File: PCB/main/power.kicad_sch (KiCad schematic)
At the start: 25 parts, among them IC1 MCP6002T-I_SN, IC2 ap2007, IC3 TP4056-42-ESOP8, IC4 LM3940IMP-3.3_NOPB, Q1 AO3401A

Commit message: Updated footprints
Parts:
- IC1: footprint SOIC127P600X175-8N -> EEE3088F_Footprints:SOIC127P600X175-8N
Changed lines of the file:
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@@
       (effects (font (size 1.27 1.27)) (justify left))
     )
-    (property "Footprint" "SOIC127P600X175-8N" (id 2) (at 97.155 132.08 0)
+    (property "Footprint" "EEE3088F_Footprints:SOIC127P600X175-8N" (id 2) (at 97.155 132.08 0)
       (effects (font (size 1.27 1.27)) (justify left) hide)
     )

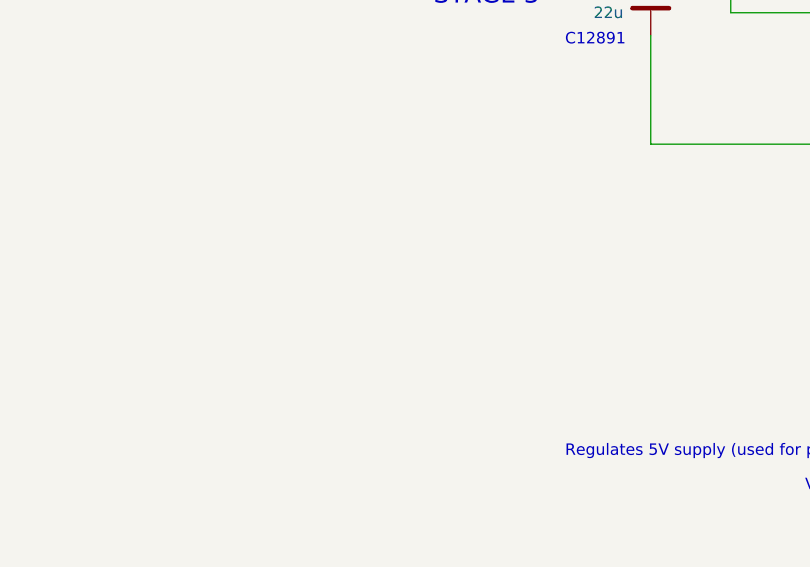
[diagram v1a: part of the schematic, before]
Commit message: Fixed a lot of shit. Added 3 test pads. Rounded PCB corners
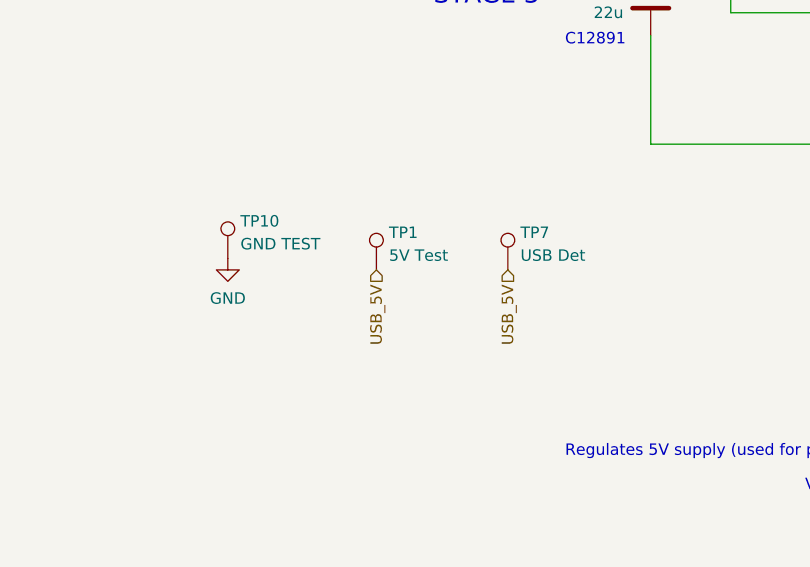
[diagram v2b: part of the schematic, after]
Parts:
- added TP1: 5V Test, TestPoint:TestPoint_Pad_2.5x2.5mm, symbol Connector:TestPoint
- added TP10: GND TEST, TestPoint:TestPoint_Pad_4.0x4.0mm, symbol Connector:TestPoint
- added TP7: USB Det, TestPoint:TestPoint_Pad_2.5x2.5mm, symbol Connector:TestPoint
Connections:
- net GND: now also TP10.1
- net USB_5V: now also TP1.1, TP7.1
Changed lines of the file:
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@@
     (effects (font (size 1.27 1.27)) (justify left))
   )
+  (hierarchical_label "USB_5V" (shape input) (at 161.29 95.885 270)
+    (effects (font (size 1.27 1.27)) (justify right))
+  )
   (hierarchical_label "5V" (shape input) (at 205.74 130.81 180)
     (effects (font (size 1.27 1.27)) (justify right))
@@
   )
   (hierarchical_label "GND" (shape input) (at 236.22 83.82 270)
+    (effects (font (size 1.27 1.27)) (justify right))
+  )
+  (hierarchical_label "USB_5V" (shape input) (at 175.895 95.885 270)
     (effects (font (size 1.27 1.27)) (justify right))
   )
@@
     (pin "2")
   )
+  (symbol (lib_id "Connector:TestPoint") (at 161.29 95.885 0) (unit 1)
+    (in_bom yes) (on_board yes) (fields_autoplaced)
+    (property "Reference" "TP1" (id 0) (at 162.687 91.7483 0)
+      (effects (font (size 1.27 1.27)) (justify left))
+    )
+    (property "Value" "5V Test" (id 1) (at 162.687 94.2852 0)
+      (effects (font (size 1.27 1.27)) (justify left))
+    )
+    (property "Footprint" "TestPoint:TestPoint_Pad_2.5x2.5mm" (id 2) (at 166.37 95.885 0)
+      (effects (font (size 1.27 1.27)) hide)
+    )
+    (property "Datasheet" "~" (id 3) (at 166.37 95.885 0)
+      (effects (font (size 1.27 1.27)) hide)
+    )
+    (pin "1")
+  )
   (symbol (lib_id "Device:LED") (at 43.18 50.8 90) (unit 1)
     (in_bom yes) (on_board yes)
@@
     (pin "1")
     (pin "2")
+  )
+  (symbol (lib_id "power:GND") (at 144.78 94.615 0) (unit 1)
+    (in_bom yes) (on_board yes) (fields_autoplaced)
+    (property "Reference" "#PWR0101" (id 0) (at 144.78 100.965 0)
+      (effects (font (size 1.27 1.27)) hide)
+    )
+    (property "Value" "GND" (id 1) (at 144.78 99.0584 0))
+    (property "Footprint" "" (id 2) (at 144.78 94.615 0)
+      (effects (font (size 1.27 1.27)) hide)
+    )
+    (property "Datasheet" "" (id 3) (at 144.78 94.615 0)
+      (effects (font (size 1.27 1.27)) hide)
+    )
+    (pin "1")
+  )
+  (symbol (lib_id "Connector:TestPoint") (at 144.78 94.615 0) (unit 1)
+    (in_bom yes) (on_board yes) (fields_autoplaced)
+    (property "Reference" "TP10" (id 0) (at 146.177 90.4783 0)
+      (effects (font (size 1.27 1.27)) (justify left))
+    )
+    (property "Value" "GND TEST" (id 1) (at 146.177 93.0152 0)
+      (effects (font (size 1.27 1.27)) (justify left))
+    )
+    (property "Footprint" "TestPoint:TestPoint_Pad_4.0x4.0mm" (id 2) (at 149.86 94.615 0)
+      (effects (font (size 1.27 1.27)) hide)
+    )
+    (property "Datasheet" "~" (id 3) (at 149.86 94.615 0)
+      (effects (font (size 1.27 1.27)) hide)
+    )
+    (pin "1")
   )
   (symbol (lib_id "AO3401A:AO3401A") (at 78.105 125.73 90) (unit 1)
@@
     (pin "2")
   )
+  (symbol (lib_id "Connector:TestPoint") (at 175.895 95.885 0) (unit 1)
+    (in_bom yes) (on_board yes) (fields_autoplaced)
+    (property "Reference" "TP7" (id 0) (at 177.292 91.7483 0)
+      (effects (font (size 1.27 1.27)) (justify left))
+    )
+    (property "Value" "USB Det" (id 1) (at 177.292 94.2852 0)
+      (effects (font (size 1.27 1.27)) (justify left))
+    )
+    (property "Footprint" "TestPoint:TestPoint_Pad_2.5x2.5mm" (id 2) (at 180.975 95.885 0)
+      (effects (font (size 1.27 1.27)) hide)
+    )
+    (property "Datasheet" "~" (id 3) (at 180.975 95.885 0)
+      (effects (font (size 1.27 1.27)) hide)
+    )
+    (pin "1")
+  )
   (symbol (lib_id "Device:R") (at 50.8 43.18 0) (unit 1)

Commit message: Updated PCB with testpads
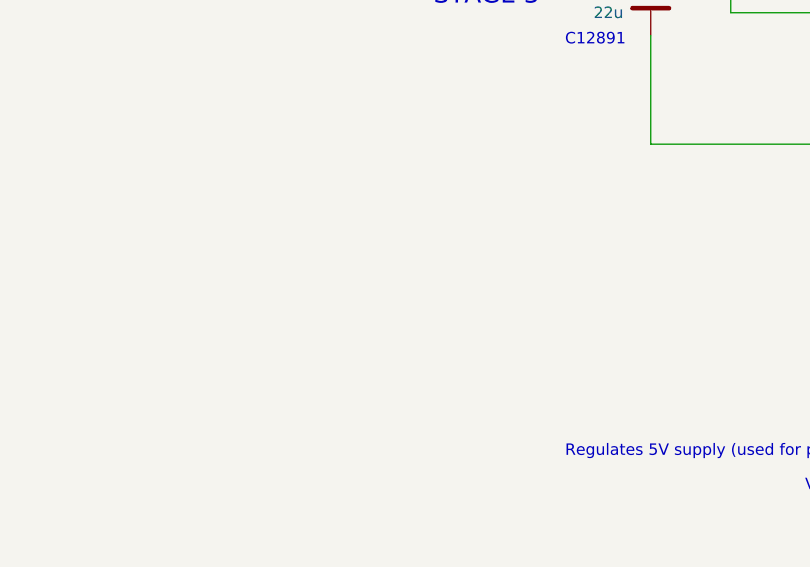
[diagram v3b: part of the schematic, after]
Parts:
- removed TP1: 5V Test, TestPoint:TestPoint_Pad_2.5x2.5mm, symbol Connector:TestPoint
- removed TP10: GND TEST, TestPoint:TestPoint_Pad_4.0x4.0mm, symbol Connector:TestPoint
- removed TP7: USB Det, TestPoint:TestPoint_Pad_2.5x2.5mm, symbol Connector:TestPoint
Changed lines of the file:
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@@
     (effects (font (size 1.27 1.27)) (justify left))
   )
-  (hierarchical_label "USB_5V" (shape input) (at 161.29 95.885 270)
-    (effects (font (size 1.27 1.27)) (justify right))
-  )
   (hierarchical_label "5V" (shape input) (at 205.74 130.81 180)
     (effects (font (size 1.27 1.27)) (justify right))
@@
   )
   (hierarchical_label "GND" (shape input) (at 236.22 83.82 270)
-    (effects (font (size 1.27 1.27)) (justify right))
-  )
-  (hierarchical_label "USB_5V" (shape input) (at 175.895 95.885 270)
     (effects (font (size 1.27 1.27)) (justify right))
   )
@@
     (pin "2")
   )
-  (symbol (lib_id "Connector:TestPoint") (at 161.29 95.885 0) (unit 1)
-    (in_bom yes) (on_board yes) (fields_autoplaced)
-    (property "Reference" "TP1" (id 0) (at 162.687 91.7483 0)
-      (effects (font (size 1.27 1.27)) (justify left))
-    )
-    (property "Value" "5V Test" (id 1) (at 162.687 94.2852 0)
-      (effects (font (size 1.27 1.27)) (justify left))
-    )
-    (property "Footprint" "TestPoint:TestPoint_Pad_2.5x2.5mm" (id 2) (at 166.37 95.885 0)
-      (effects (font (size 1.27 1.27)) hide)
-    )
-    (property "Datasheet" "~" (id 3) (at 166.37 95.885 0)
-      (effects (font (size 1.27 1.27)) hide)
-    )
-    (pin "1")
-  )
   (symbol (lib_id "Device:LED") (at 43.18 50.8 90) (unit 1)
     (in_bom yes) (on_board yes)
@@
     (pin "1")
     (pin "2")
-  )
-  (symbol (lib_id "power:GND") (at 144.78 94.615 0) (unit 1)
-    (in_bom yes) (on_board yes) (fields_autoplaced)
-    (property "Reference" "#PWR0101" (id 0) (at 144.78 100.965 0)
-      (effects (font (size 1.27 1.27)) hide)
-    )
-    (property "Value" "GND" (id 1) (at 144.78 99.0584 0))
-    (property "Footprint" "" (id 2) (at 144.78 94.615 0)
-      (effects (font (size 1.27 1.27)) hide)
-    )
-    (property "Datasheet" "" (id 3) (at 144.78 94.615 0)
-      (effects (font (size 1.27 1.27)) hide)
-    )
-    (pin "1")
-  )
-  (symbol (lib_id "Connector:TestPoint") (at 144.78 94.615 0) (unit 1)
-    (in_bom yes) (on_board yes) (fields_autoplaced)
-    (property "Reference" "TP10" (id 0) (at 146.177 90.4783 0)
-      (effects (font (size 1.27 1.27)) (justify left))
-    )
-    (property "Value" "GND TEST" (id 1) (at 146.177 93.0152 0)
-      (effects (font (size 1.27 1.27)) (justify left))
-    )
-    (property "Footprint" "TestPoint:TestPoint_Pad_4.0x4.0mm" (id 2) (at 149.86 94.615 0)
-      (effects (font (size 1.27 1.27)) hide)
-    )
-    (property "Datasheet" "~" (id 3) (at 149.86 94.615 0)
-      (effects (font (size 1.27 1.27)) hide)
-    )
-    (pin "1")
   )
   (symbol (lib_id "AO3401A:AO3401A") (at 78.105 125.73 90) (unit 1)
@@
     (pin "2")
   )
-  (symbol (lib_id "Connector:TestPoint") (at 175.895 95.885 0) (unit 1)
-    (in_bom yes) (on_board yes) (fields_autoplaced)
-    (property "Reference" "TP7" (id 0) (at 177.292 91.7483 0)
-      (effects (font (size 1.27 1.27)) (justify left))
-    )
-    (property "Value" "USB Det" (id 1) (at 177.292 94.2852 0)
-      (effects (font (size 1.27 1.27)) (justify left))
-    )
-    (property "Footprint" "TestPoint:TestPoint_Pad_2.5x2.5mm" (id 2) (at 180.975 95.885 0)
-      (effects (font (size 1.27 1.27)) hide)
-    )
-    (property "Datasheet" "~" (id 3) (at 180.975 95.885 0)
-      (effects (font (size 1.27 1.27)) hide)
-    )
-    (pin "1")
-  )
   (symbol (lib_id "Device:R") (at 50.8 43.18 0) (unit 1)

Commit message: Finished Gerbers and updated BOM
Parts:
- removed Q1: AO3401A, EEE3088F_Footprints:SOT95P280X125-3N, symbol AO3401A:AO3401A
- added Q1: LBSS84LT1G, EEE3088F_Footprints:SOT96P237X111-3N, symbol LBSS84LT1G:LBSS84LT1G
- C1, C3, C8: value 22u -> 22uF; LCSC (none) -> C12891
- C2, C4, C7: value 10u -> 10uF; LCSC (none) -> C13585
- C5: value 0.47u -> 0.47uF; LCSC (none) -> C47339
- C6: value 1u -> 1.0uF; LCSC (none) -> C28323
- D1: LCSC (none) -> C72043
- D2: LCSC (none) -> C84256
- D3: LCSC (none) -> C8598
- IC1: LCSC (none) -> C7377
- IC2: LCSC (none) -> C130338
- IC3: LCSC (none) -> C16581
- IC4: LCSC (none) -> C140319
- L1: LCSC (none) -> C408336
- R1, R2, R7: LCSC (none) -> C22765
- R3, R4: LCSC (none) -> C17928
- R5: LCSC (none) -> C17900
- R6: footprint EEE3088F_Footprints:RESC2013X65N -> EEE3088F_Footprints:R0603; LCSC (none) -> C4216
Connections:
- net V_UVLO: now also Q1.3
- net at IC1.1 (VOUTA): now also Q1.1
- net at D3.1 (K), IC1.8 (VDD): now also Q1.2
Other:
- note added: "C8492"
- note removed: "C15127"

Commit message: Updated Gerbers and DNPs
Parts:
- BT1: Populate (none) -> DNP
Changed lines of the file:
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@@
+      (effects (font (size 1.27 1.27)) hide)
+    )
+    (property "Populate" "DNP" (id 4) (at 151.765 31.115 0)
       (effects (font (size 1.27 1.27)) hide)
     )
